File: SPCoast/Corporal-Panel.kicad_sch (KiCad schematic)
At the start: 16 parts, among them U12031 0x2A, U12032 0x2B

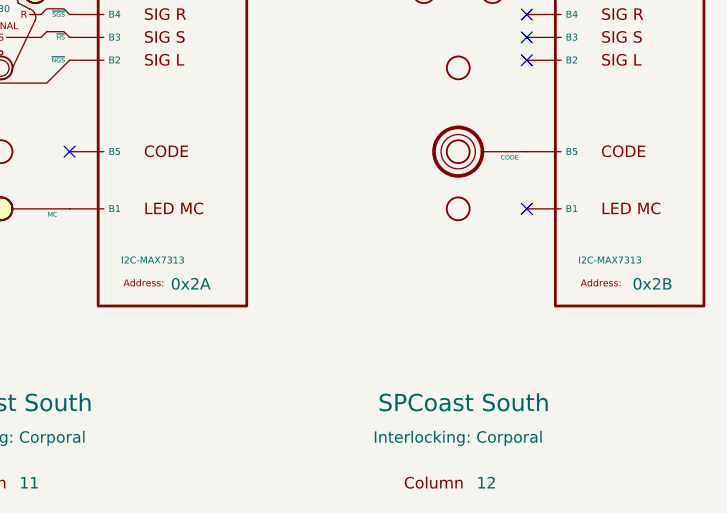
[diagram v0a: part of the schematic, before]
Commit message: chore(kicad): SPCoast symbols refreshed, field attribute visibility, no-connects on unused pins (owner's edit, baseline)
Owner, 2026-10-08: updated symbols from the libraries (the field pin direction flip, InterlockingPlant
61269e0), adjusted attribute visibility, added 22 no-connect markers on unused pins.

Verified (committed as saved, no edits):
- 485 components, 648 nets; every net identical to the previous commit.
- ERC 53 -> 20 messages (13 errors, 7 warnings). Remaining: unconnected HOUSE H / aux MC pins
  (Gilroy Caltrain, Luchessa, Watsonville); Corporal SW11901 still Railroad:Switch_HandThrow (not in
  the library) with open N/R legs; Sargent switch 1 open N/R legs; Christopher Panel U10029 A6 open
  while lamp LMP10093 carries a no-connect; 5 inherited wire stubs.
- Every instance path starts at the root uuid.

Co-Authored-By: Claude Opus 5.5 <noreply@anthropic.com>
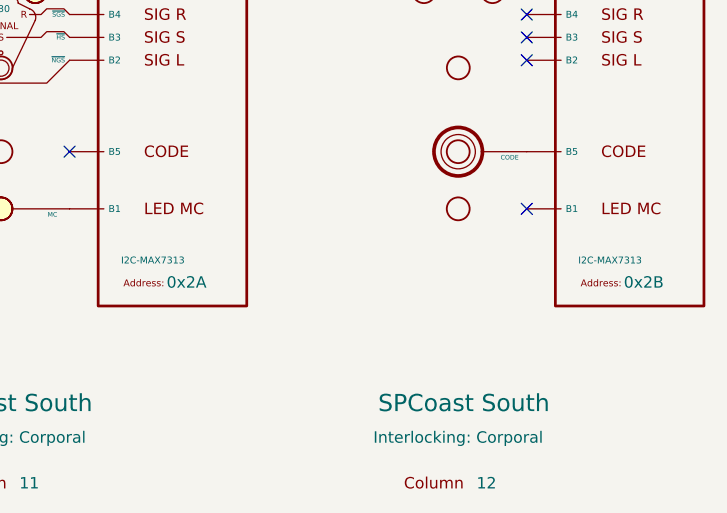
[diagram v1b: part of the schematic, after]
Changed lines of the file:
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@@
+			)
+		)
+		(property "LAMP" ""
+			(at 80.01 26.67 0)
+			(hide yes)
+			(show_name no)
+			(do_not_autoplace no)
+			(effects
+				(font
+					(size 1.27 1.27)
+				)
 			)
 		)
@@
 			)
 		)
+		(property "LAMP" ""
+			(at 130.81 36.83 0)
+			(hide yes)
+			(show_name no)
+			(do_not_autoplace no)
+			(effects
+				(font
+					(size 1.27 1.27)
+				)
+			)
+		)
 		(pin "1"
 		)
@@
 			(at 93.345 109.855 0)
 			(show_name no)
-			(do_not_autoplace no)
+			(do_not_autoplace yes)
 			(effects
 				(font
@@
 		)
 		(property "Address" "0x2A"
-			(at 101.092 112.522 0)
+			(at 100.6281 112.3109 0)
 			(show_name no)
 			(do_not_autoplace no)
@@
 			)
 		)
+		(property "LAMP" ""
+			(at 80.01 36.83 0)
+			(hide yes)
+			(show_name no)
+			(do_not_autoplace no)
+			(effects
+				(font
+					(size 1.27 1.27)
+				)
+			)
+		)
 		(pin "1"
 		)
@@
 			)
 		)
+		(property "LAMP" ""
+			(at 80.01 104.14 0)
+			(hide yes)
+			(show_name no)
+			(do_not_autoplace no)
+			(effects
+				(font
+					(size 1.27 1.27)
+				)
+			)
+		)
 		(pin "1"
 		)
@@
 			)
 		)
+		(property "LAMP" ""
+			(at 130.81 26.67 0)
+			(hide yes)
+			(show_name no)
+			(do_not_autoplace no)
+			(effects
+				(font
+					(size 1.27 1.27)
+				)
+			)
+		)
 		(pin "1"
 		)
@@
 			(at 144.145 109.855 0)
 			(show_name no)
-			(do_not_autoplace no)
+			(do_not_autoplace yes)
 			(effects
 				(font
@@
 		)
 		(property "Address" "0x2B"
-			(at 152.4 112.522 0)
+			(at 151.4281 112.3109 0)
 			(show_name no)
 			(do_not_autoplace no)
@@
 			)
 		)
+		(property "NWS" ""
+			(at 130.81 63.5 0)
+			(hide yes)
+			(show_name no)
+			(do_not_autoplace no)
+			(effects
+				(font
+					(size 1.27 1.27)
+				)
+			)
+		)
+		(property "RWS" ""
+			(at 130.81 63.5 0)
+			(hide yes)
+			(show_name no)
+			(do_not_autoplace no)
+			(effects
+				(font
+					(size 1.27 1.27)
+				)
+			)
+		)
+		(property "RWK" ""
+			(at 130.81 63.5 0)
+			(hide yes)
+			(show_name no)
+			(do_not_autoplace no)
+			(effects
+				(font
+					(size 1.27 1.27)
+				)
+			)
+		)
+		(property "NWK" ""
+			(at 130.81 63.5 0)
+			(hide yes)
+			(show_name no)
+			(do_not_autoplace no)
+			(effects
+				(font
+					(size 1.27 1.27)
+				)
+			)
+		)
 		(pin "1"
 		)
@@
 			)
 		)
+		(property "LAMP" ""
+			(at 130.81 31.75 0)
+			(hide yes)
+			(show_name no)
+			(do_not_autoplace no)
+			(effects
+				(font
+					(size 1.27 1.27)
+				)
+			)
+		)
 		(pin "1"
 		)
@@
 			)
 		)
+		(property "LAMP" ""
+			(at 80.01 31.75 0)
+			(hide yes)
+			(show_name no)
+			(do_not_autoplace no)
+			(effects
+				(font
+					(size 1.27 1.27)
+				)
+			)
+		)
 		(pin "1"
 		)
@@
 			)
 		)
+		(property "WLS" ""
+			(at 80.01 63.5 0)
+			(hide yes)
+			(show_name no)
+			(do_not_autoplace no)
+			(effects
+				(font
+					(size 1.27 1.27)
+				)
+			)
+		)
+		(property "WLK" ""
+			(at 80.01 63.5 0)
+			(hide yes)
+			(show_name no)
+			(do_not_autoplace no)
+			(effects
+				(font
+					(size 1.27 1.27)
+				)
+			)
+		)
 		(pin "1"
 		)
@@
 			)
 		)
+		(property "SW" ""
+			(at 80.01 48.26 0)
+			(hide yes)
+			(show_name no)
+			(do_not_autoplace no)
+			(effects
+				(font
+					(size 1.27 1.27)
+				)
+			)
+		)
 		(pin "1"
 		)
@@
 			)
 		)
+		(property "NGS" ""
+			(at 80.01 83.82 0)
+			(hide yes)
+			(show_name no)
+			(do_not_autoplace no)
+			(effects
+				(font
+					(size 1.27 1.27)
+				)
+			)
+		)
+		(property "HS" ""
+			(at 80.01 83.82 0)
+			(hide yes)
+			(show_name no)
+			(do_not_autoplace no)
+			(effects
+				(font
+					(size 1.27 1.27)
+				)
+			)
+		)
+		(property "SGS" ""
+			(at 80.01 83.82 0)
+			(hide yes)
+			(show_name no)
+			(do_not_autoplace no)
+			(effects
+				(font
+					(size 1.27 1.27)
+				)
+			)
+		)
+		(property "SGK" ""
+			(at 80.01 83.82 0)
+			(hide yes)
+			(show_name no)
+			(do_not_autoplace no)
+			(effects
+				(font
+					(size 1.27 1.27)
+				)
+			)
+		)
+		(property "NGK" ""
+			(at 80.01 83.82 0)
+			(hide yes)
+			(show_name no)
+			(do_not_autoplace no)
+			(effects
+				(font
+					(size 1.27 1.27)
+				)
+			)
+		)
+		(property "TEK" ""
+			(at 80.01 83.82 0)
+			(hide yes)
+			(show_name no)
+			(do_not_autoplace no)
+			(effects
+				(font
+					(size 1.27 1.27)
+				)
+			)
+		)
 		(pin "1"
 		)
@@
 			(hide yes)
 			(show_name no)
+			(do_not_autoplace no)
+			(effects
+				(font
+					(size 1.27 1.27)
+				)
+			)
+		)
+		(property "CODE" ""
+			(at 130.81 97.79 0)
+			(hide yes)
+			(show_name no)

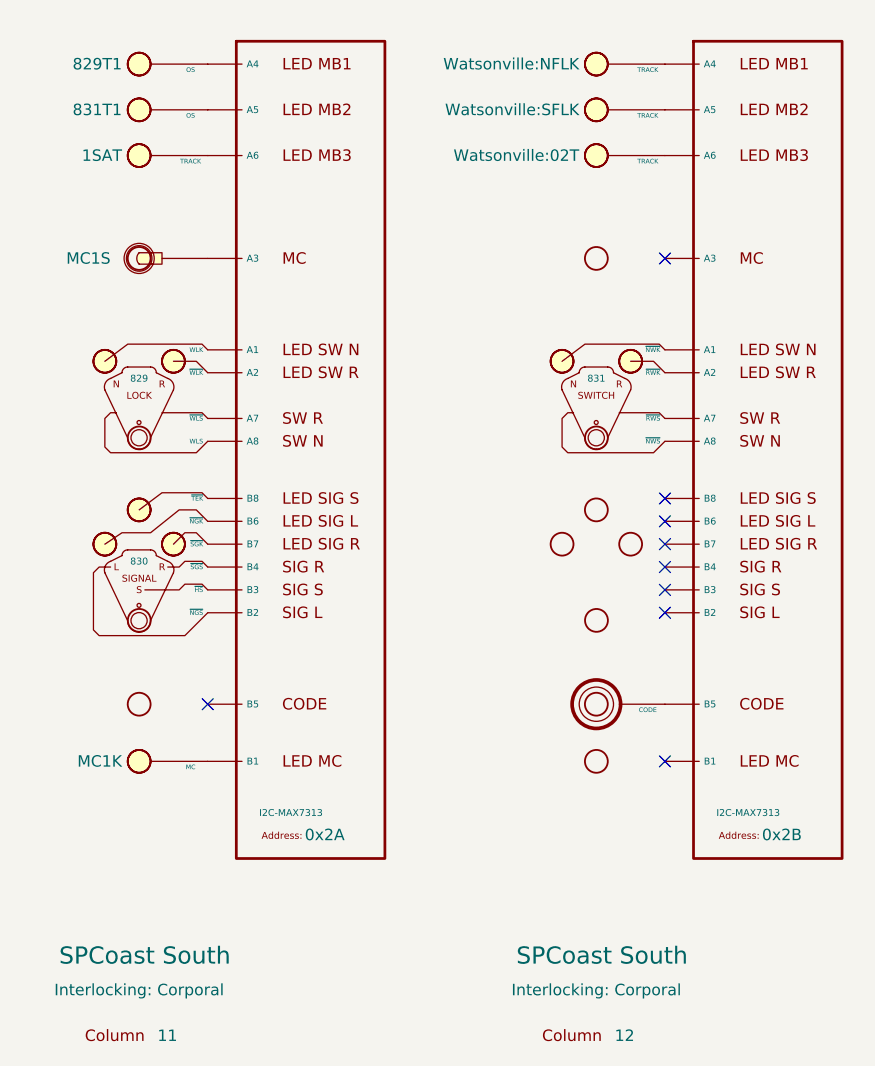
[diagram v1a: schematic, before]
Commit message: feat(spcoast): every sheet on the four Railroad libraries (checkpoint step 6, mechanical half)
By SPCoast/edits/2026-10-12-migrate-libraries.py, run once with KiCad closed: 483 instances
remapped across 16 sheets, embedded definitions replaced by the library blocks, instance fields
synced (Kind, ControlToken, Vital, NormalIs, Chain, Index dropped; Indications renamed
IndicationCeiling; Hold_ms renamed hold_ms; a pixel's Index became its Address; Rulebook kept
on the four Luchessa markers because the compiler still reads it), and 22 units added at the
same position for the plates and devices that are multi-unit now. Owner's choices: every plant
head CPL; Sargent's semaphore UQ; the 0x27 PCA9685 as PWM; the office MAX7313s as the
SPCoastcTc variant. Left by hand: the two AUXILIARY_TRAFFIC markers on Watsonville (retired).

Verified (production/migration-gate.txt, netlist_diff.py against pre-migration.net): office
and local plates and all chips keep their connectivity; 14 nets lost, all on Sargent, where
the six field devices (DevSW13001, 13004 to 13007, 13012) have new pin positions and must be
re-wired by hand. ERC: lib_symbol_issues 492 before (unregistered libraries) to 2 after (the
retired markers); the 29 unconnected pins are those devices and their chip pins.

Co-Authored-By: Claude Fable 5.1 <noreply@anthropic.com>
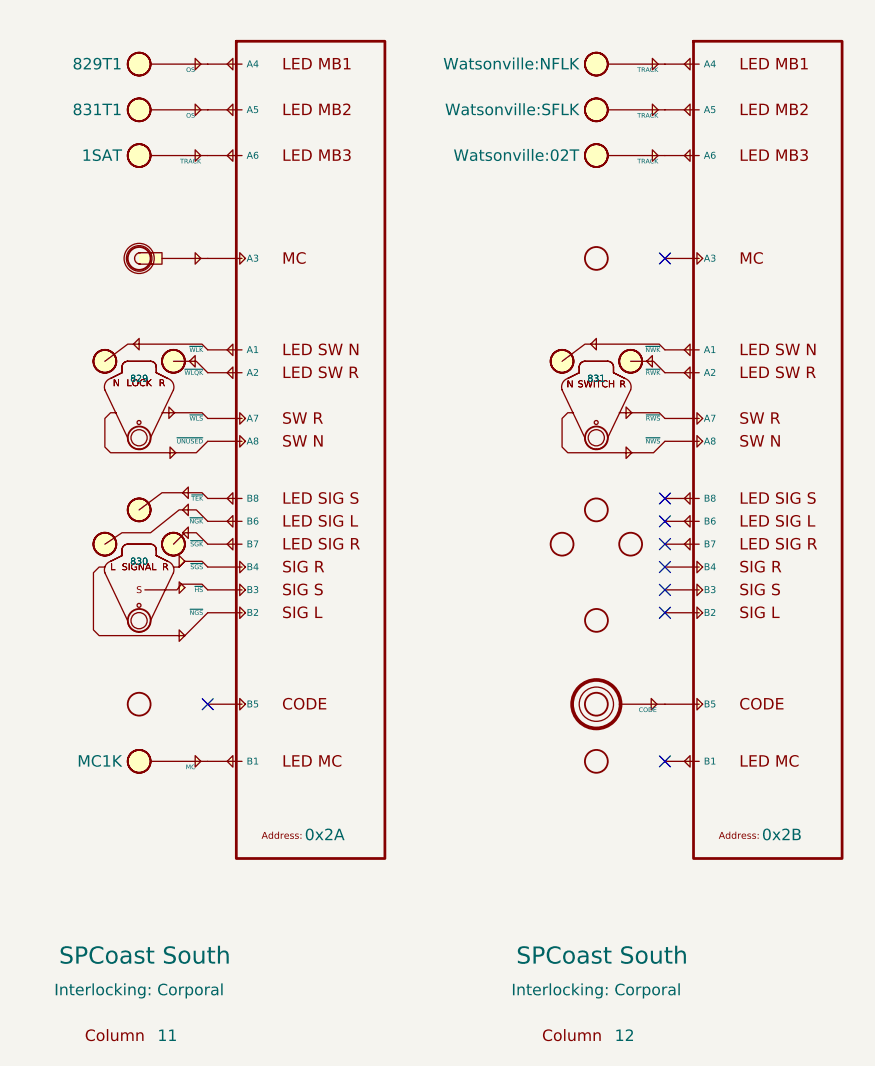
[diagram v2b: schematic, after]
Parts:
- added unit 2 of LKL12011
- added unit 2 of SGL12011
- added unit 2 of SWL12012
- CDE12012: symbol RailroadPanel:PanelCode -> Railroad-Office:PanelCode; Appliance (none) -> lever; Kind CODE -> (none); Pin.CODE (none) -> binary; Style (none) -> code
- COL12031, COL12032: symbol RailroadPanel:PanelColumn -> Railroad-Office:PanelColumn
- LKL12011: symbol RailroadPanel:PanelLock -> Railroad-Office:PanelLock; Appliance (none) -> lever; Invert (none) -> WLK; Kind LOCK_LEVER_2LAMP_2CONTACT -> (none); Pin.UNUSED (none) -> binary; Pin.WLK (none) -> binary; Pin.WLQK (none) -> binary; Pin.WLS (none) -> binary; Style (none) -> lock
- LMP12111, LMP12113, LMP12123, MCK12011: symbol RailroadPanel:PanelLamp-YELLOW -> Railroad-Office:PanelLamp-YELLOW; Appliance (none) -> lamp; Kind LAMP -> (none); Pin.LAMP (none) -> binary; Style (none) -> indication
- LMP12112: symbol RailroadPanel:PanelLamp-RED -> Railroad-Office:PanelLamp-RED; Appliance (none) -> lamp; Kind LAMP -> (none); Pin.LAMP (none) -> binary; Style (none) -> indication
- LMP12121, LMP12122: symbol RailroadPanel:PanelLamp-BLUE -> Railroad-Office:PanelLamp-BLUE; Appliance (none) -> lamp; Kind LAMP -> (none); Pin.LAMP (none) -> binary; Style (none) -> indication
- MCL12011: symbol RailroadPanel:PanelMCall -> Railroad-Office:PanelMCall; Appliance (none) -> lever; ControlToken MC1S -> (none); Kind MAINTAINER_CALL -> (none); Pin.S (none) -> binary; Style (none) -> maintainer_call; Vital NO -> (none)
- SGL12011: symbol RailroadPanel:PanelSignal -> Railroad-Office:PanelSignal; Appliance (none) -> lever; Kind SIGNAL_LEVER -> (none); Pin.HS (none) -> binary; Pin.NGK (none) -> binary; Pin.NGS (none) -> binary; Pin.SGK (none) -> binary; Pin.SGS (none) -> binary; Pin.TEK (none) -> binary; Style (none) -> signal
- SWL12012: symbol RailroadPanel:PanelSwitch -> Railroad-Office:PanelSwitch; Appliance (none) -> lever; Kind SWITCH_LEVER -> (none); Pin.NWK (none) -> binary; Pin.NWS (none) -> binary; Pin.RWK (none) -> binary; Pin.RWS (none) -> binary; Style (none) -> switch
- U12031, U12032: symbol RailroadPanel:Driver-I2C-MAX7313 -> Railroad-HardwareIO:Driver-I2C-MAX7313-SPCoastcTc; IC (none) -> MAX7313; Kind I2C-MAX7313 -> (none); Pin.A1 (none) -> binary; Pin.A2 (none) -> binary; Pin.A3 (none) -> binary; Pin.A4 (none) -> binary; Pin.A5 (none) -> binary; Pin.A6 (none) -> binary; Pin.A7 (none) -> binary; Pin.A8 (none) -> binary; Pin.B1 (none) -> binary; Pin.B2 (none) -> binary; Pin.B3 (none) -> binary; Pin.B4 (none) -> binary; Pin.B5 (none) -> binary; Pin.B6 (none) -> binary; Pin.B7 (none) -> binary; Pin.B8 (none) -> binary
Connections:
- net at U12031.1 (A1): now also LKL12011.5 (~{WLK}); no longer LKL12011.5 (WLK)
- net at U12031.14 (B6): now also SGL12011.6 (~{NGK}); no longer SGL12011.6 (~{NGK})
- net at U12031.15 (B7): now also SGL12011.5 (~{SGK}); no longer SGL12011.5 (~{SGK})
- net at U12031.16 (B8): now also SGL12011.7 (~{TEK}); no longer SGL12011.7 (~{TEK})
- net at U12031.2 (A2): now also LKL12011.4 (~{WLQK}); no longer LKL12011.4 (~{WLK})
- net at U12032.1 (A1): now also SWL12012.5 (~{NWK}); no longer SWL12012.5 (~{NWK})
- net at U12032.2 (A2): now also SWL12012.4 (~{RWK}); no longer SWL12012.4 (~{RWK})

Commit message: chore: owner's Sargent cleanup and library edits of 2026-10-12 and 13 (baseline)
Co-Authored-By: Claude Fable 5.1 <noreply@anthropic.com>
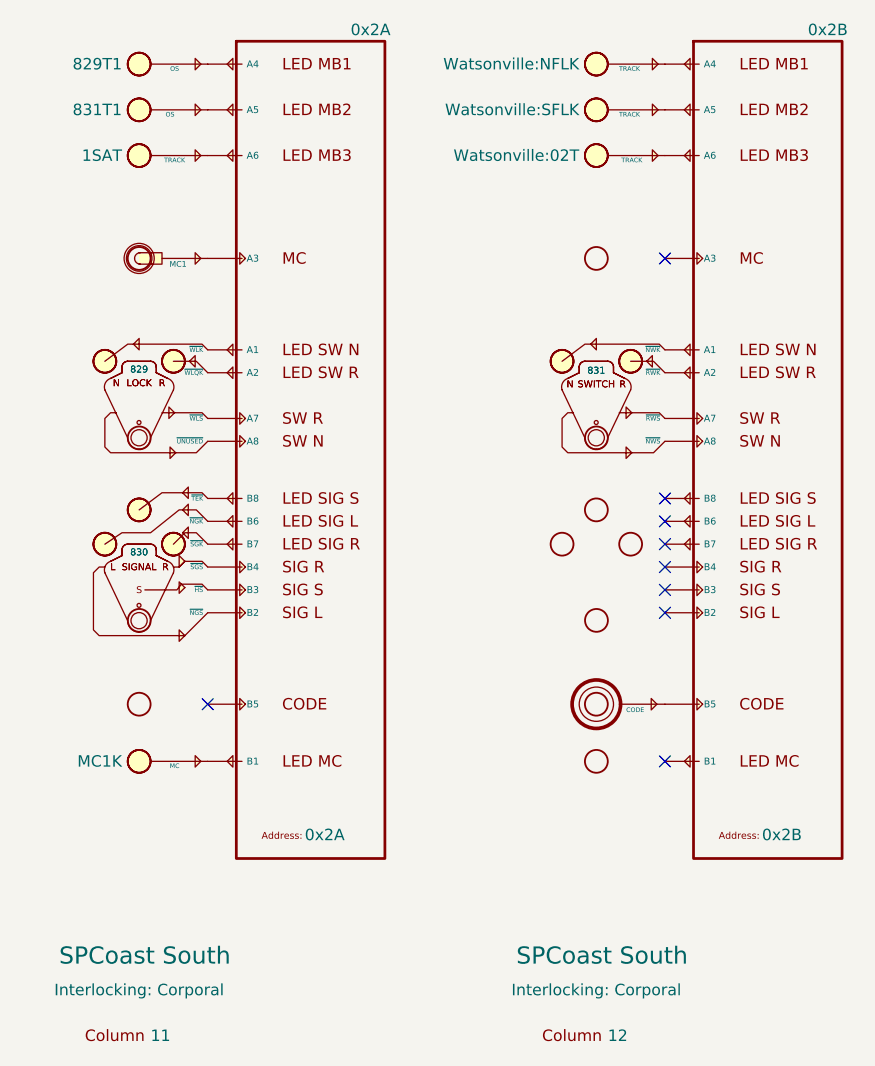
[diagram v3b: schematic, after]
